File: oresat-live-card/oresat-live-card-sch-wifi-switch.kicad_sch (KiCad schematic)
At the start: 40 parts, among them J11 2X1_TH_JUMPER, J15 2X1_TH_JUMPER, U24 LTC6994-1, U25 LTC6994-1, U26 SN74LVC1G32QDBVRQ1, U30 SN74LV1T34DBV, U32 SN74LV1T34, U34 QPC1022, U35 SN74LVC1G32QDBVRQ1, U36 QPC1022, U6 NC7SVU04P5X

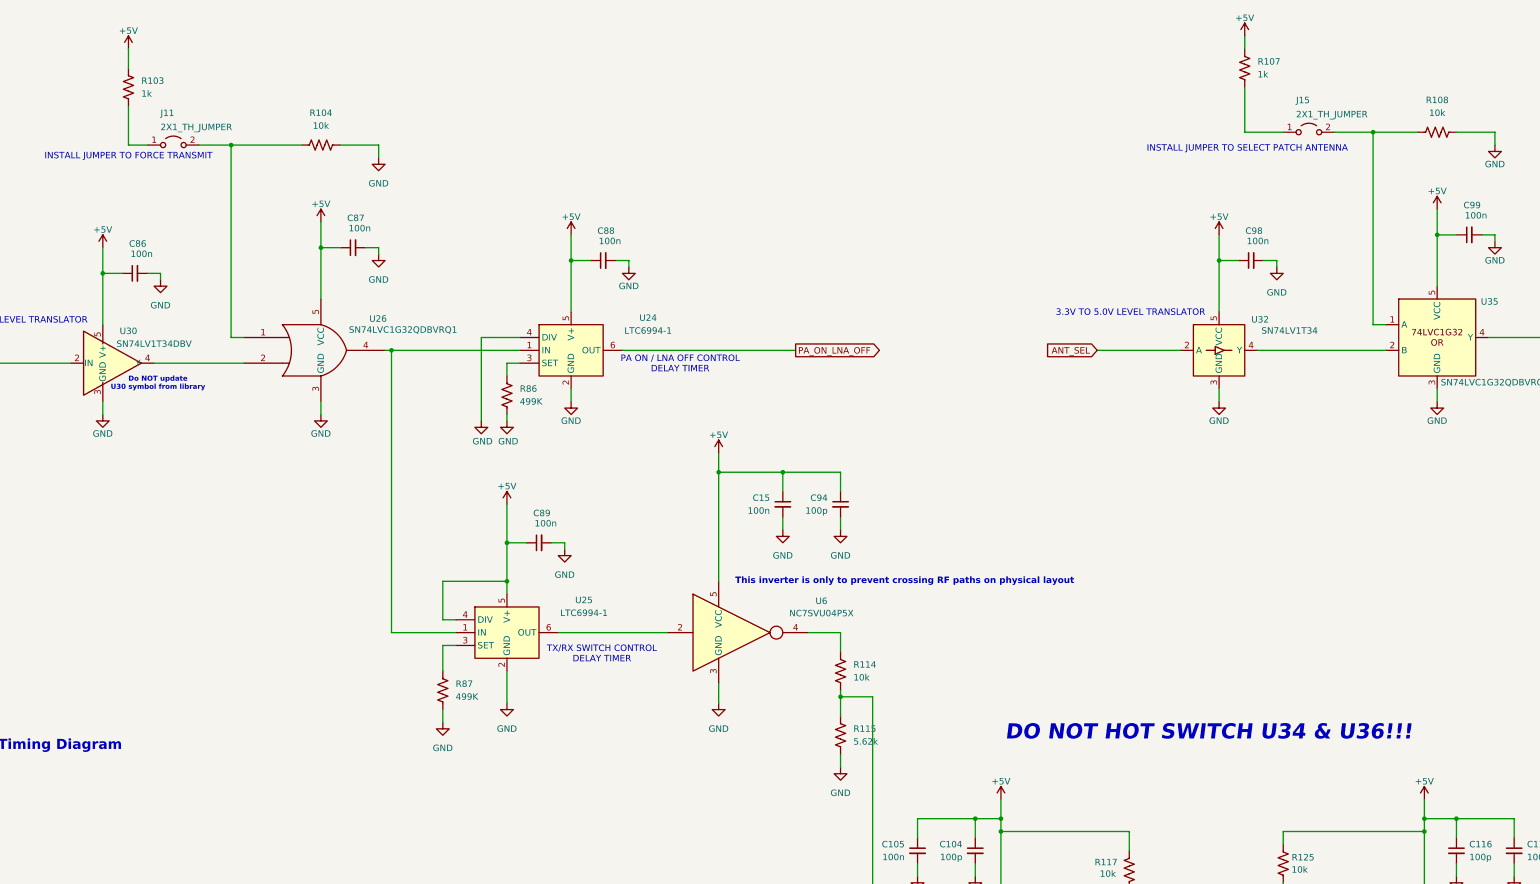
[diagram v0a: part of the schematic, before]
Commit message: Moved WiFi switch to 5VA, making the entire RF subsystem powered off that one supply. Fixed up RF path, still need to remove solder mask.
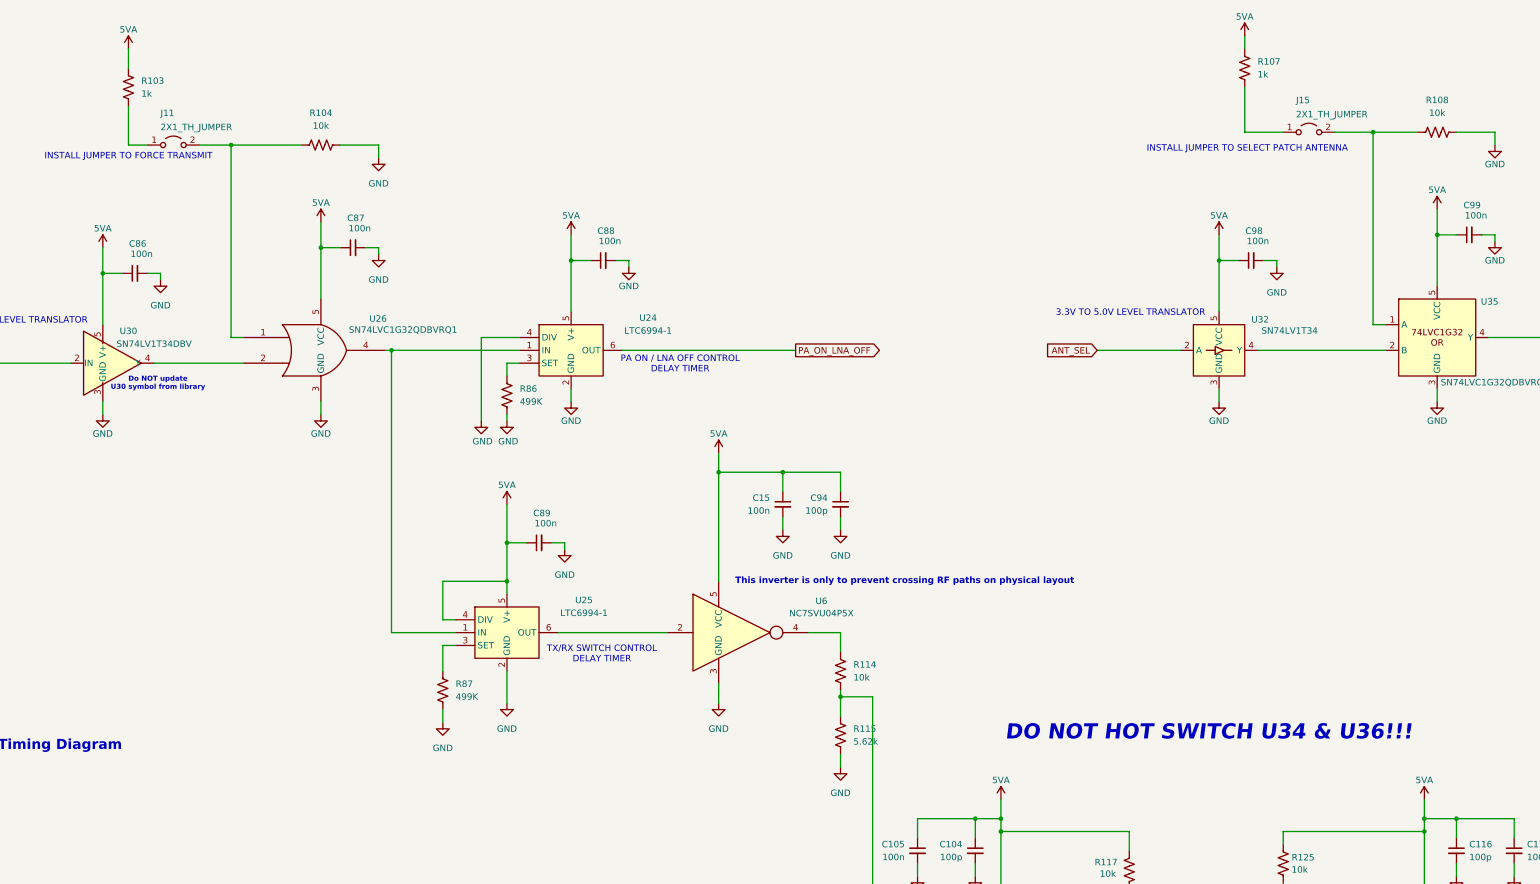
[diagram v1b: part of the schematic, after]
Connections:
- net +5V renamed 5VA

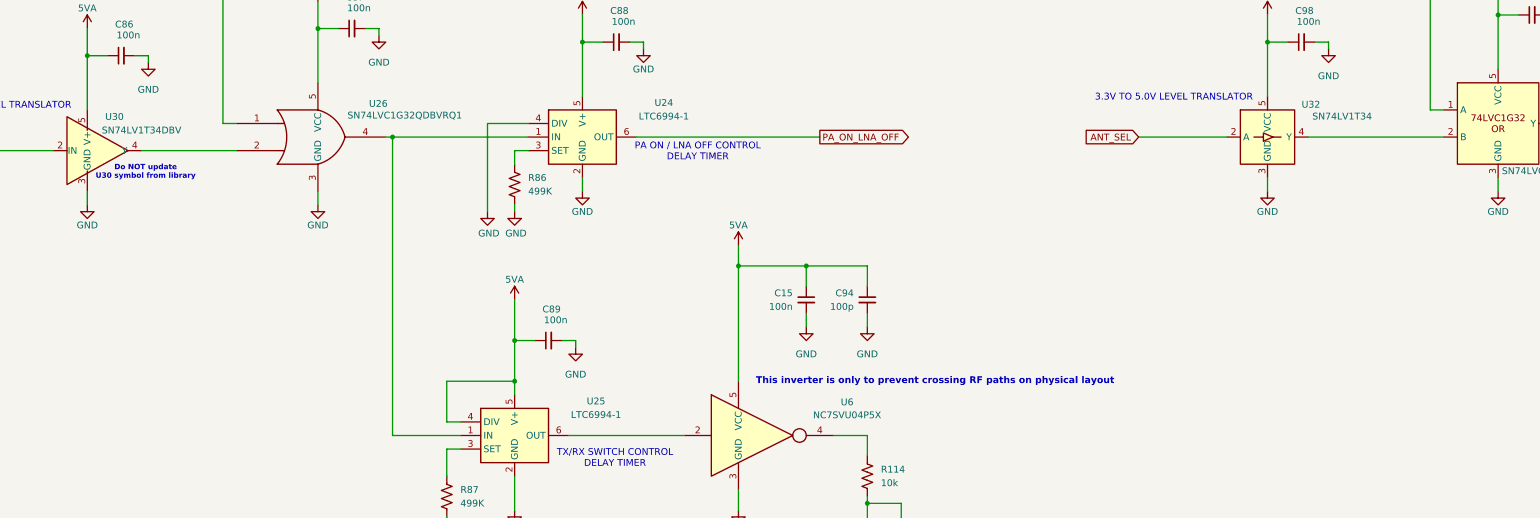
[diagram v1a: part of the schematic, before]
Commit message: added Olivers BOM and footprint changes, cleaned up pcb
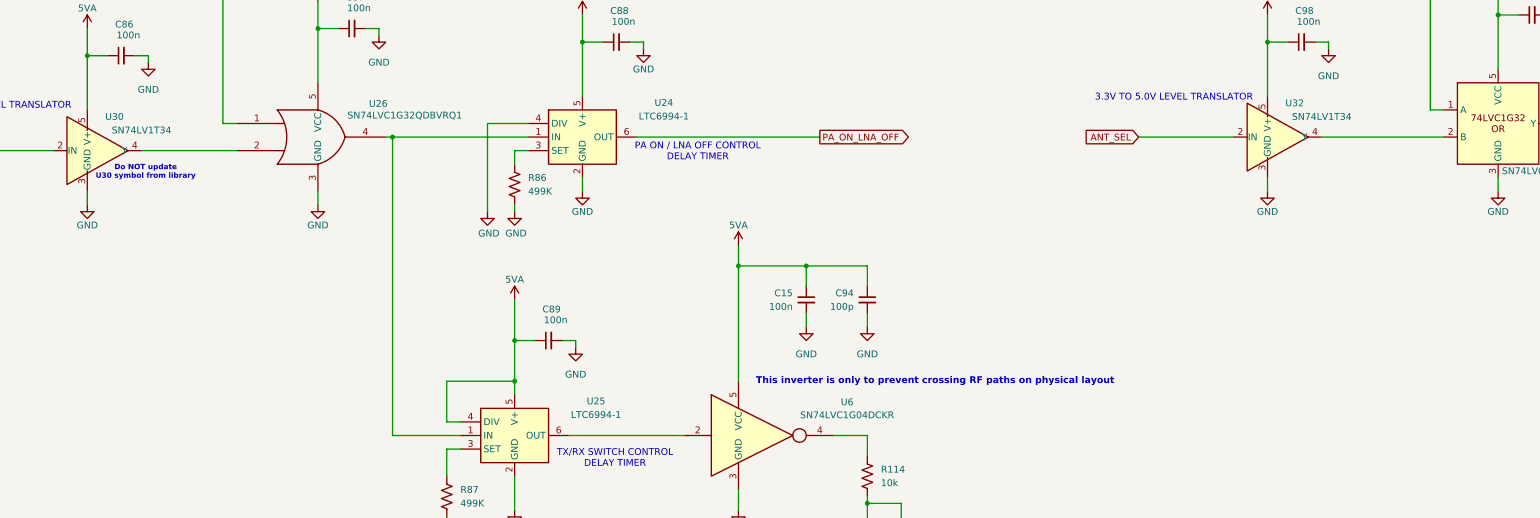
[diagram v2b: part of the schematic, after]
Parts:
- removed U32: SN74LV1T34, Package_TO_SOT_SMD:SOT-353_SC-70-5, symbol Logic_LevelTranslator:SN74LV1T34DCK
- added U32: SN74LV1T34, Package_TO_SOT_SMD:SOT-353_SC-70-5, symbol Amplifier_Buffer:LM6321H
- C103, C104, C115, C117, C94: footprint Resistor_SMD:R_0402_1005Metric -> oresat-passives:0402-C
- C105, C15, C86, R87: footprint oresat-passives:0402-C -> oresat-passives:0603-C
- C116: footprint Capacitor_SMD:C_0402_1005Metric -> oresat-passives:0402-C
- C118: footprint Capacitor_SMD:C_0402_1005Metric -> oresat-passives:0603-C
- C87, C88, C89, C98, C99, R103, R104, R107, R108, R114, R115, R122, R123, R86: footprint Resistor_SMD:R_0603_1608Metric -> oresat-passives:0603-C
- R116: DPN P5.62KHCT-ND -> P5.62KLCT-ND; MPN ERJ-3EKF5621V -> ERJ-2RKF5621X
- R117: DPN P10.0KHCT-ND -> P10.0KLCT-ND; MPN ERJ-3EKF1002V -> ERJ-2RKF1002X
- R124: footprint Resistor_SMD:R_0402_1005Metric -> oresat-passives:0402-C; DPN P5.62KHCT-ND -> P5.62KLCT-ND; MPN ERJ-3EKF5621V -> ERJ-2RKF5621X
- R125: footprint Resistor_SMD:R_0402_1005Metric -> oresat-passives:0402-C; DPN P10.0KHCT-ND -> P10.0KLCT-ND; MPN ERJ-3EKF1002V -> ERJ-2RKF1002X
- U24, U25: DIS (none) -> DigiKey
- U26, U35: DIS (none) -> DigiKey; DPN (none) -> 296-24202-1-ND; MFR (none) -> Texas Instruments; MPN (none) -> SN74LVC1G32QDBVRQ1
- U30: value SN74LV1T34DBV -> SN74LV1T34; footprint Package_TO_SOT_SMD:SOT-23-5 -> Package_TO_SOT_SMD:SOT-353_SC-70-5
- U6: value NC7SVU04P5X -> SN74LVC1G04DCKR; footprint Package_TO_SOT_SMD:SC-74A-5_1.55x2.9mm_P0.95mm -> oresat-live-card:C70(TI-DCK); DIS (none) -> DigiKey; DPN (none) -> 296-11600-1-ND; MFR (none) -> Texas Instruments; MPN (none) -> SN74LVC1G04DCKR
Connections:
- net 5VA: now also U32.5 (V+)
- net ANT_SEL: now also U32.2 (IN)
- net GND: now also U32.3 (GND)
- net at U35.2 (B): now also U32.4 (Y)

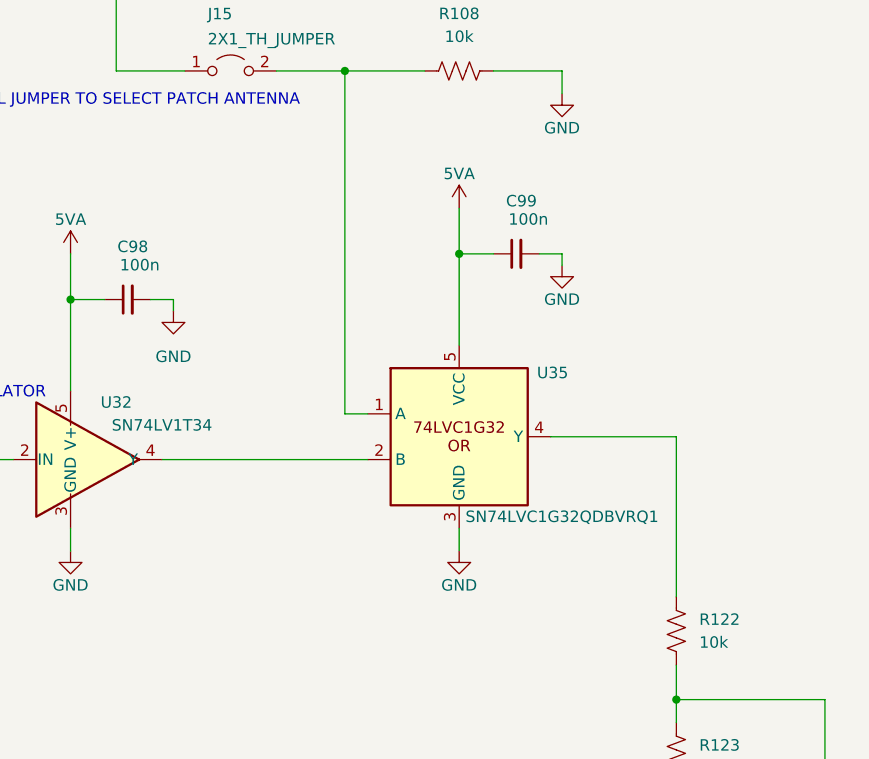
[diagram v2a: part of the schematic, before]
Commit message: updated symbol of U35
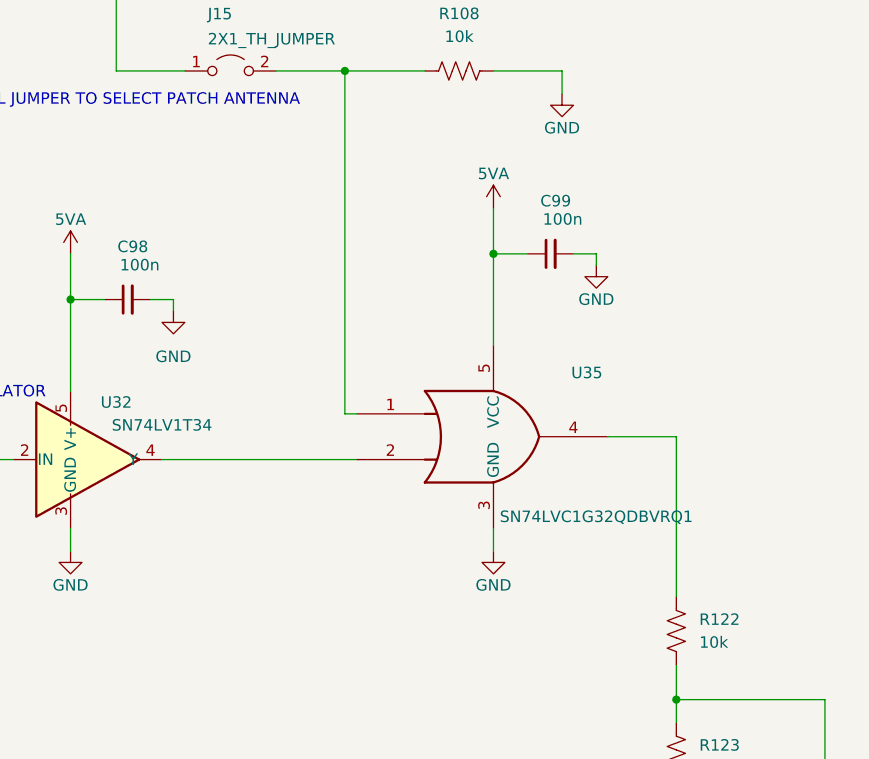
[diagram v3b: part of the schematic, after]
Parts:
- U35: symbol oresat-ics:SN74LVC1G32QDBVRQ1 -> 74xGxx:74LVC1G32
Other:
- moved on the sheet: C99, U35
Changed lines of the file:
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@@
 	)
 	(junction
-		(at 325.12 68.58)
+		(at 328.93 68.58)
 		(diameter 0)
 		(color 0 0 0 0)
@@
 	(wire
 		(pts
+			(xy 341.63 88.9) (xy 349.25 88.9)
+		)
+		(stroke
+			(width 0)
+			(type default)
+		)
+	)
+	(wire
+		(pts
 			(xy 281.94 99.06) (xy 281.94 101.6)
 		)
@@
 	(wire
 		(pts
-			(xy 334.01 68.58) (xy 336.55 68.58)
+			(xy 337.82 68.58) (xy 340.36 68.58)
 		)
 		(stroke
@@
 	(wire
 		(pts
-			(xy 312.42 86.36) (xy 314.96 86.36)
-		)
-		(stroke
-			(width 0)
-			(type default)
-		)
-	)
-	(wire
-		(pts
 			(xy 349.25 118.11) (xy 365.76 118.11)
 		)
@@
 	(wire
 		(pts
-			(xy 335.28 88.9) (xy 349.25 88.9)
-		)
-		(stroke
-			(width 0)
-			(type default)
-		)
-	)
-	(wire
-		(pts
 			(xy 294.64 196.85) (xy 294.64 199.39)
 		)
@@
 	(wire
 		(pts
-			(xy 325.12 99.06) (xy 325.12 101.6)
+			(xy 328.93 99.06) (xy 328.93 101.6)
 		)
 		(stroke
@@
 	(wire
 		(pts
-			(xy 325.12 68.58) (xy 325.12 78.74)
+			(xy 328.93 68.58) (xy 328.93 78.74)
 		)
 		(stroke
@@
 	(wire
 		(pts
-			(xy 336.55 69.85) (xy 336.55 68.58)
+			(xy 340.36 69.85) (xy 340.36 68.58)
 		)
 		(stroke
@@
 	(wire
 		(pts
-			(xy 325.12 68.58) (xy 328.93 68.58)
+			(xy 328.93 68.58) (xy 332.74 68.58)
 		)
 		(stroke
@@
 	(wire
 		(pts
-			(xy 325.12 63.5) (xy 325.12 68.58)
+			(xy 328.93 63.5) (xy 328.93 68.58)
 		)
 		(stroke
@@
 	(wire
 		(pts
+			(xy 312.42 86.36) (xy 313.69 86.36)
+		)
+		(stroke
+			(width 0)
+			(type default)
+		)
+	)
+	(wire
+		(pts
 			(xy 207.01 115.57) (xy 207.01 119.38)
 		)
@@
 	(wire
 		(pts
-			(xy 292.1 91.44) (xy 314.96 91.44)
+			(xy 292.1 91.44) (xy 313.69 91.44)
 		)
 		(stroke
@@
 	(symbol
 		(lib_id "power:GND")
-		(at 325.12 101.6 0)
+		(at 328.93 101.6 0)
 		(unit 1)
 		(exclude_from_sim no)
@@
 		(dnp no)
 		(property "Reference" "#PWR0199"
-			(at 325.12 107.95 0)
+			(at 328.93 107.95 0)
 			(effects
 				(font
@@
 		)
 		(property "Value" "GND"
-			(at 325.12 105.41 0)
+			(at 328.93 105.41 0)
 			(effects
 				(font
@@
 		)
 		(property "Footprint" ""
-			(at 325.12 101.6 0)
+			(at 328.93 101.6 0)
 			(effects
 				(font
@@
 		)
 		(property "Datasheet" ""
-			(at 325.12 101.6 0)
+			(at 328.93 101.6 0)
 			(effects
 				(font
@@
 		)
 		(property "Description" "Power symbol creates a global label with name \"GND\" , ground"
-			(at 325.12 101.6 0)
+			(at 328.93 101.6 0)
 			(effects
 				(font
@@
 	)
 	(symbol
-		(lib_id "oresat-ics:SN74LVC1G32QDBVRQ1")
-		(at 325.12 88.9 0)
+		(lib_id "74xGxx:74LVC1G32")
+		(at 328.93 88.9 0)
 		(unit 1)
 		(exclude_from_sim no)
@@
 		(dnp no)
 		(property "Reference" "U35"
-			(at 333.756 82.55 0)
+			(at 337.566 82.55 0)
 			(effects
 				(font
@@
 		)
 		(property "Value" "SN74LVC1G32QDBVRQ1"
-			(at 336.55 97.79 0)
+			(at 340.36 97.79 0)
 			(effects
 				(font
@@
 		)
 		(property "Footprint" "Package_TO_SOT_SMD:SOT-23-5"
-			(at 325.12 83.82 0)
+			(at 328.93 88.9 0)
 			(effects
 				(font
@@
 			)
 		)
-		(property "Datasheet" "https://www.ti.com/lit/ds/symlink/sn74lvc1g32-q1.pdf?HQS=dis-dk-null-digikeymode-dsf-pf-null-wwe&ts=1759274623820&ref_url=https%253A%252F%252Fwww.ti.com%252Fgeneral%252Fdocs%252Fsuppproductinfo.tsp%253FdistId%253D10%2526gotoUrl%253Dhttps%253A%252F%252Fwww.ti.com%252Flit%252Fgpn%252Fsn74lvc1g32-q1"
-			(at 325.12 83.82 0)
+		(property "Datasheet" "http://www.ti.com/lit/sg/scyt129e/scyt129e.pdf"
+			(at 328.93 88.9 0)
 			(effects
 				(font
@@
 			)
 		)
-		(property "Description" "IC GATE OR 1CH 2-INP SOT23-5"
-			(at 325.12 88.9 0)
+		(property "Description" "Single OR Gate, Low-Voltage CMOS"
+			(at 328.93 88.9 0)
 			(effects
 				(font
@@
 		)
 		(property "DIS" "DigiKey"
-			(at 325.12 88.9 0)
+			(at 328.93 88.9 0)
 			(effects
 				(font
@@
 		)
 		(property "DPN" "296-24202-1-ND"
-			(at 325.12 88.9 0)
+			(at 328.93 88.9 0)
 			(effects
 				(font
@@
 		)
 		(property "MFR" "Texas Instruments"
-			(at 325.12 88.9 0)
+			(at 328.93 88.9 0)
 			(effects
 				(font
@@
 		)
 		(property "MPN" "SN74LVC1G32QDBVRQ1"
-			(at 325.12 88.9 0)
+			(at 328.93 88.9 0)
 			(effects
 				(font
@@
 	(symbol
 		(lib_id "power:GND")
-		(at 336.55 69.85 0)
+		(at 340.36 69.85 0)
 		(unit 1)
 		(exclude_from_sim no)
@@
 		(dnp no)
 		(property "Reference" "#PWR0201"
-			(at 336.55 76.2 0)
+			(at 340.36 76.2 0)
 			(effects
 				(font
@@
 		)
 		(property "Value" "GND"
-			(at 336.55 73.66 0)
+			(at 340.36 73.66 0)
 			(effects
 				(font
@@
 		)
 		(property "Footprint" ""
-			(at 336.55 69.85 0)
+			(at 340.36 69.85 0)
 			(effects
 				(font
@@
 		)
 		(property "Datasheet" ""
-			(at 336.55 69.85 0)
+			(at 340.36 69.85 0)
 			(effects
 				(font
@@
 		)
 		(property "Description" "Power symbol creates a global label with name \"GND\" , ground"
-			(at 336.55 69.85 0)
+			(at 340.36 69.85 0)
 			(effects
 				(font
@@
 	(symbol
 		(lib_id "Device:C_Small")
-		(at 331.47 68.58 90)
+		(at 335.28 68.58 90)
 		(unit 1)
 		(exclude_from_sim no)
@@
 		(dnp no)
 		(property "Reference" "C99"
-			(at 333.756 61.976 90)
+			(at 337.566 61.976 90)
 			(effects
 				(font
@@
 		)
 		(property "Value" "100n"
-			(at 335.026 64.008 90)
+			(at 338.836 64.008 90)
 			(effects
 				(font
@@
 		)
 		(property "Footprint" "oresat-passives:0603-C"
-			(at 331.47 68.58 0)
+			(at 335.28 68.58 0)
 			(effects
 				(font
@@
 		)
 		(property "Datasheet" ""
-			(at 331.47 68.58 0)
+			(at 335.28 68.58 0)
 			(effects
 				(font
@@
 		)
 		(property "Description" "CAP CER 0.1UF 25V X7R 0603"
-			(at 331.47 68.58 0)
+			(at 335.28 68.58 0)
 			(effects
 				(font
@@
 		)
 		(property "MPN" "CGA3E2X7R1E104K080AA "
-			(at 331.47 68.58 0)
+			(at 335.28 68.58 0)
 			(effects
 				(font
@@
 		)
 		(property "DPN" "445-5667-1-ND "
-			(at 331.47 68.58 90)
+			(at 335.28 68.58 90)
 			(effects
 				(font
@@
 		)
 		(property "MFR" "TDK Corporation "
-			(at 331.47 68.58 90)
+			(at 335.28 68.58 90)
 			(effects
 				(font
@@
 		)
 		(property "DIS" "DigiKey"
-			(at 331.47 68.58 90)
+			(at 335.28 68.58 90)
 			(effects
 				(font
@@
 	(symbol
 		(lib_id "oresat-power:5VA")
-		(at 325.12 63.5 0)
+		(at 328.93 63.5 0)
 		(unit 1)
 		(exclude_from_sim no)
@@
 		(dnp no)
 		(property "Reference" "#5VA014"
-			(at 325.12 67.31 0)
+			(at 328.93 67.31 0)
 			(effects
 				(font
@@
 		)
 		(property "Value" "5VA"
-			(at 325.12 59.69 0)
+			(at 328.93 59.69 0)
 			(effects
 				(font
@@
 		)
 		(property "Footprint" ""
-			(at 325.12 63.5 0)
+			(at 328.93 63.5 0)
 			(effects
 				(font
@@
 		)
 		(property "Datasheet" ""
-			(at 325.12 63.5 0)
+			(at 328.93 63.5 0)
 			(effects
 				(font
@@
 		)
 		(property "Description" ""
-			(at 325.12 63.5 0)
+			(at 328.93 63.5 0)
 			(effects
 				(font
